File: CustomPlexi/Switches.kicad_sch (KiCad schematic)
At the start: 3 parts, among them SW1 Plexi Channel Select, SW2 Plexi Enable/Disable

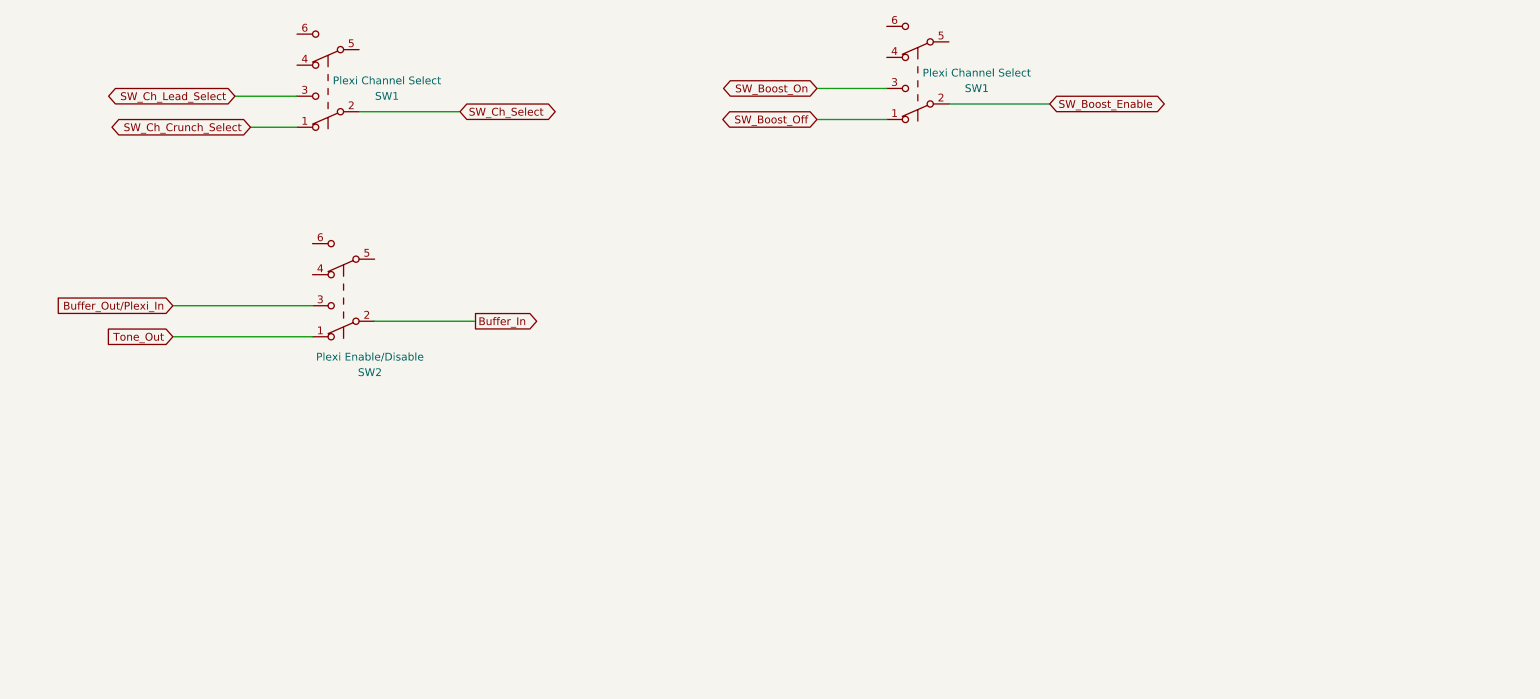
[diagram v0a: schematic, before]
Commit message: Signal chain ok except separated volumes
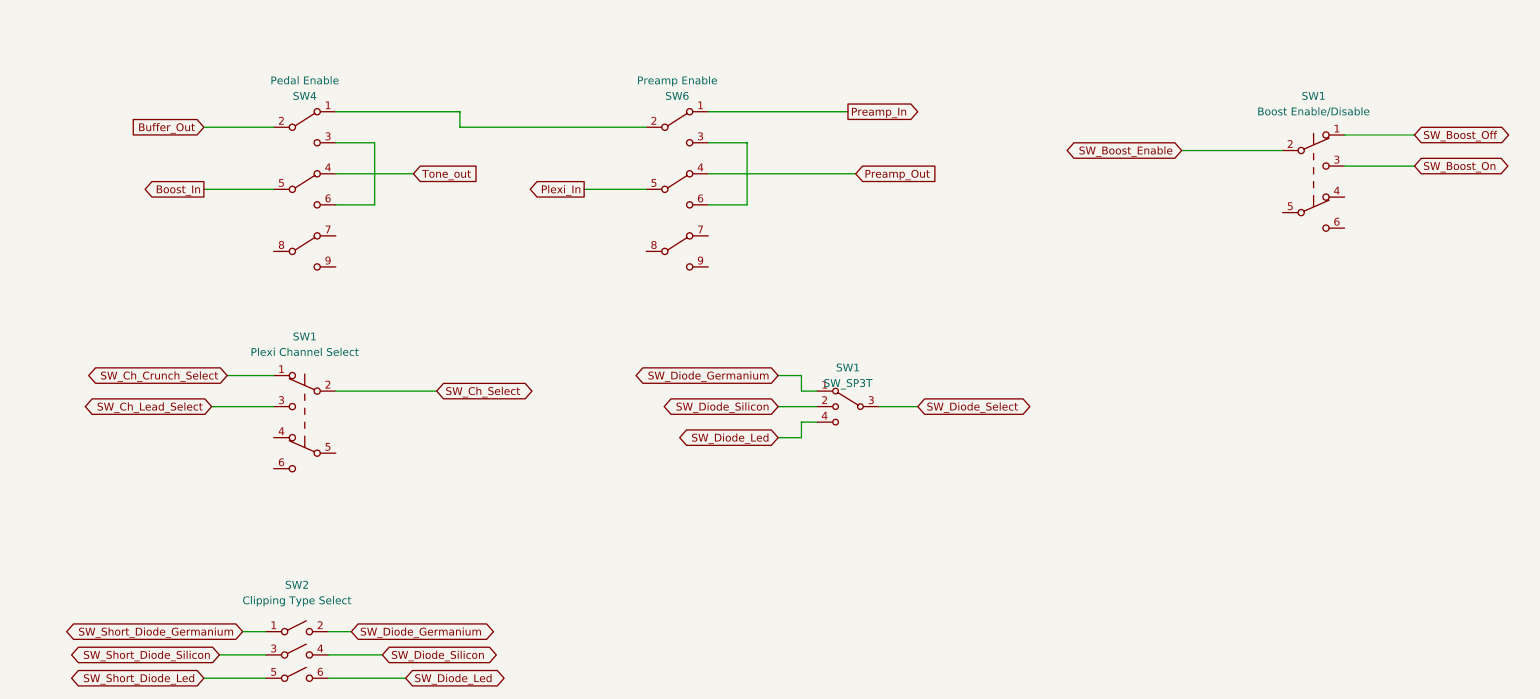
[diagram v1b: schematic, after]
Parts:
- removed SW2: Plexi Enable/Disable, symbol Switch:SW_Push_DPDT
- added SW1: SW_SP3T, symbol Switch:SW_SP3T
- added SW2: Clipping Type Select, symbol CustomLib:SW_3PST
- added SW4: Pedal Enable, symbol CustomLib:SW_3PDT
- added SW6: Preamp Enable, symbol CustomLib:SW_3PDT
- SW1: value Plexi Channel Select -> Boost Enable/Disable
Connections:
- new net: SW4.1, SW6.2
- new net: SW6.3, SW6.6
- new net: SW4.3, SW4.6
- new net Boost_In: SW4.5
- new net Buffer_Out: SW4.2
- new net Plexi_In: SW6.5
- new net Preamp_In: SW6.1
- new net Preamp_Out: SW6.4
- new net SW_Diode_Germanium: SW1.1, SW2.2
- new net SW_Diode_Led: SW1.4, SW2.6
- new net SW_Diode_Select: SW1.3
- new net SW_Diode_Silicon: SW1.2, SW2.4
- new net SW_Short_Diode_Germanium: SW2.1
- new net SW_Short_Diode_Led: SW2.5
- new net SW_Short_Diode_Silicon: SW2.3
- new net Tone_out: SW4.4
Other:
- moved on the sheet: SW1
